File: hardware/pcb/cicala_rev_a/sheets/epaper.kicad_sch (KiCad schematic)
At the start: 23 parts, among them J2 FH12-24S-0.5SH, Q1 Si1308EDL, U6 TPS22917DBVR

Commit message: feat(hw): isolate the panel bus and ground the USB-C shell
The panel's logic pins could back-power an unpowered panel through its own
ESD diodes whenever firmware deasserted EPD_PWR_EN with an output still
driven. R27-R31 put 470 ohm in series with every MCU-driven panel line, which
caps the injected current at about 5.7 mA per pin against a 3.3 V output and
a diode drop. At 4 MHz into roughly 20 pF of connector and trace the added
rise time is about 21 ns, so the same parts double as the series-tuning
positions the review asked for; fit 0 ohm to remove them during bring-up.

R32 holds the panel in reset while EPD_3V3 is off and while the MCU pin is
high-impedance. 1 M draws 3.3 uA, and only when RESET is high, which happens
only with the panel already powered.

The nets either side of the resistors are named apart: EPD_* stays the GPIO
net that pin_contract.csv and the firmware refer to, PNL_* is the panel side.

The USB-C shell had a no-connect flag and no recorded rationale. The
enclosure is plastic and carries no chassis ground, so the shell's only
discharge path is to the board. R33 (0 ohm, fitted) makes that path direct;
C31 is the alternative for a DC-isolated shell.

Co-Authored-By: Claude Opus 5 <noreply@anthropic.com>
Claude-Session: https://claude.ai/code/session_01E5vy1HJsPztSk9nFw6j5Ko
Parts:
- added R32: 1M, Resistor_SMD:R_0603_1608Metric, symbol Device:R
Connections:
- net GND: now also R32.2
- net EPD_CLK renamed PNL_CLK
- net EPD_CS renamed PNL_CS
- net EPD_DC renamed PNL_DC
- net EPD_MOSI renamed PNL_MOSI
- net EPD_RESET renamed PNL_RESET
- net PNL_RESET: now also R32.1
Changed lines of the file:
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@@
 	(wire
 		(pts
-			(xy 30.48 149.86) (xy 33.02 149.86)
-		)
-		(stroke
-			(width 0)
-			(type default)
-		)
-	)
-	(wire
-		(pts
 			(xy 62.23 43.18) (xy 62.23 48.26)
 		)
@@
 		)
 	)
-	(global_label "EPD_MOSI"
+	(global_label "PNL_MOSI"
 		(shape passive)
 		(at 33.02 160.02 0)
@@
 		)
 	)
-	(global_label "EPD_CS"
+	(global_label "PNL_CS"
 		(shape passive)
 		(at 33.02 154.94 0)
@@
 		)
 	)
-	(global_label "EPD_CLK"
+	(global_label "PNL_CLK"
 		(shape passive)
 		(at 33.02 157.48 0)
@@
 		)
 	)
-	(global_label "EPD_DC"
+	(global_label "PNL_DC"
 		(shape passive)
 		(at 33.02 152.4 0)
@@
 		)
 	)
-	(global_label "EPD_RESET"
+	(global_label "PNL_RESET"
 		(shape passive)
-		(at 33.02 149.86 0)
+		(at 55.88 149.86 0)
 		(fields_autoplaced yes)
 		(effects
@@
 		)
 		(property "Intersheetrefs" "${INTERSHEET_REFS}"
-			(at 33.02 149.86 0)
+			(at 55.88 149.86 0)
 			(hide yes)
 			(show_name no)
@@
 				)
 			)
+		)
+	)
+	(wire
+		(pts
+			(xy 30.48 149.86) (xy 55.88 149.86)
+		)
+		(stroke
+			(width 0)
+			(type default)
+		)
+	)
+	(junction
+		(at 45.72 149.86)
+		(diameter 0)
+		(color 0 0 0 0)
+	)
+	(symbol
+		(lib_id "Device:R")
+		(at 45.72 153.67 0)
+		(unit 1)
+		(body_style 1)
+		(exclude_from_sim no)
+		(in_bom yes)
+		(on_board yes)
+		(in_pos_files yes)
+		(dnp no)
+		(property "Reference" "R32"
+			(at 41.91 151.892 0)
+			(show_name no)
+			(do_not_autoplace no)
+			(effects
+				(font
+					(size 1 1)
+				)
+			)
+		)
+		(property "Value" "1M"
+			(at 41.91 154.432 0)
+			(show_name no)
+			(do_not_autoplace no)
+			(effects
+				(font
+					(size 1 1)
+				)
+			)
+		)
+		(property "Footprint" "Resistor_SMD:R_0603_1608Metric"
+			(at 45.72 153.67 0)
+			(hide yes)
+			(show_name no)
+			(do_not_autoplace no)
+			(effects
+				(font
+					(size 1 1)
+				)
+			)
+		)
+		(property "Datasheet" "~"
+			(at 45.72 153.67 0)
+			(hide yes)
+			(show_name no)
+			(do_not_autoplace no)
+			(effects
+				(font
+					(size 1 1)
+				)
+			)
+		)
+		(property "Description" "Resistor"
+			(at 45.72 153.67 0)
+			(hide yes)
+			(show_name no)
+			(do_not_autoplace no)
+			(effects
+				(font
+					(size 1 1)
+				)
+			)
+		)
+		(pin "1"
+		)
+		(pin "2"
+		)
+		(instances
+			(project "cicala_rev_a"
+				(path "/9b5e4c31-c66f-4b64-9ff8-62a2c447d0bc/9467d62a-f8ed-46c9-a7cb-f7af887ddb15"
+					(reference "R32")
+					(unit 1)
+				)
+			)
+		)
+	)
+	(wire
+		(pts
+			(xy 45.72 157.48) (xy 45.72 160.02)
+		)
+		(stroke
+			(width 0)
+			(type default)
+		)
+	)
+	(symbol
+		(lib_id "power:GND")
+		(at 45.72 160.02 0)
+		(unit 1)
+		(body_style 1)
+		(exclude_from_sim no)
+		(in_bom yes)
+		(on_board yes)
+		(in_pos_files yes)
+		(dnp no)
+		(property "Reference" "#PWR0156"
+			(at 45.72 166.37 0)
+			(hide yes)
+			(show_name no)
+			(do_not_autoplace no)
+			(effects
+				(font
+					(size 1.27 1.27)
+				)
+			)
+		)
+		(property "Value" "GND"
+			(at 45.72 163.83 0)
+			(hide yes)
+			(show_name no)
+			(do_not_autoplace no)
+			(effects
+				(font
+					(size 1.27 1.27)
+				)
+			)
+		)
+		(property "Footprint" ""
+			(at 45.72 160.02 0)
+			(hide yes)
+			(show_name no)
+			(do_not_autoplace no)
+			(effects
+				(font
+					(size 1.27 1.27)
+				)
+			)
+		)
+		(property "Datasheet" ""
+			(at 45.72 160.02 0)
+			(hide yes)
+			(show_name no)
+			(do_not_autoplace no)
+			(effects
+				(font
+					(size 1.27 1.27)
+				)
+			)
+		)
+		(property "Description" "Power symbol creates a global label with name GND, ground"
+			(at 45.72 160.02 0)
+			(hide yes)
+			(show_name no)
+			(do_not_autoplace no)
+			(effects
+				(font
+					(size 1.27 1.27)
+				)
+			)
+		)
+		(pin "1"
+		)
+		(instances
+			(project "cicala_rev_a"
+				(path "/9b5e4c31-c66f-4b64-9ff8-62a2c447d0bc/9467d62a-f8ed-46c9-a7cb-f7af887ddb15"
+					(reference "#PWR0156")
+					(unit 1)
+				)
+			)

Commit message: feat(hw): give the panel a real symbol and name its pump rails
J2 was a generic Conn_01x24, so every panel signal was Pin_n and ERC could
not see an interface error. It is now a project GDEY0213B74 symbol carrying
the vendor pin names and electrical types: the four MCU-driven lines are
inputs, BUSY and GDR are outputs, VDDIO/VCI/VSS are power inputs. Pin
geometry is deliberately identical to Conn_01x24, so the sheet's wiring is
unchanged and the FH12-24S-0.5SH land still applies.

The pinout the sheet already had matches the vendor assignment on all 24
pins, including BS1 tied low for 4-wire SPI and VPP and the temperature-sensor
pair left open.

EPD_PREVGH and EPD_PREVGL are renamed EPD_VGH and EPD_VGL. They are not
pre-pump nodes: D3 rectifies the boost switch node into panel pin 21, and D1
with the C16 flying capacitor pumps panel pin 23 negative. The old names
describe the wrong side of the circuit, and one earlier wiring error on this
exact node was made easier by them.

Co-Authored-By: Claude Opus 5 <noreply@anthropic.com>
Claude-Session: https://claude.ai/code/session_01E5vy1HJsPztSk9nFw6j5Ko
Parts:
- J2: value FH12-24S-0.5SH -> GDEY0213B74; symbol Connector_Generic:Conn_01x24 -> Cicala:GDEY0213B74
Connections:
- net EPD_PREVGH renamed EPD_VGH
- net EPD_PREVGL renamed EPD_VGL
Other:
- moved on the sheet: J2
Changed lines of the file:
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@@
 		)
 	)
-	(global_label "EPD_PREVGL"
+	(global_label "EPD_VGL"
 		(shape passive)
 		(at 237.49 142.24 90)
@@
 		)
 	)
-	(global_label "EPD_PREVGH"
+	(global_label "EPD_VGH"
 		(shape passive)
 		(at 139.7 57.15 180)
@@
 		)
 	)
-	(global_label "EPD_PREVGH"
+	(global_label "EPD_VGH"
 		(shape passive)
 		(at 33.02 177.8 0)
@@
 		)
 	)
-	(global_label "EPD_PREVGL"
+	(global_label "EPD_VGL"
 		(shape passive)
 		(at 153.67 91.44 0)
@@
 		)
 	)
-	(global_label "EPD_PREVGH"
+	(global_label "EPD_VGH"
 		(shape passive)
 		(at 267.97 113.03 90)
@@
 		)
 	)
-	(global_label "EPD_PREVGL"
+	(global_label "EPD_VGL"
 		(shape passive)
 		(at 33.02 182.88 0)
@@
 	)
 	(symbol
-		(lib_id "Connector_Generic:Conn_01x24")
+		(lib_id "Cicala:GDEY0213B74")
 		(at 25.4 154.94 0)
 		(mirror y)
@@
 			)
 		)
-		(property "Value" "FH12-24S-0.5SH"
+		(property "Value" "GDEY0213B74"
 			(at 25.146 189.23 0)
 			(show_name no)
@@
 			)
 		)
-		(property "Description" "Generic connector, single row, 01x24, script generated (kicad-library-utils/schlib/autogen/connector/)"
+		(property "Description" "Panel and its FH12-24S-0.5SH board connector"
 			(at 25.4 154.94 0)
 			(hide yes)

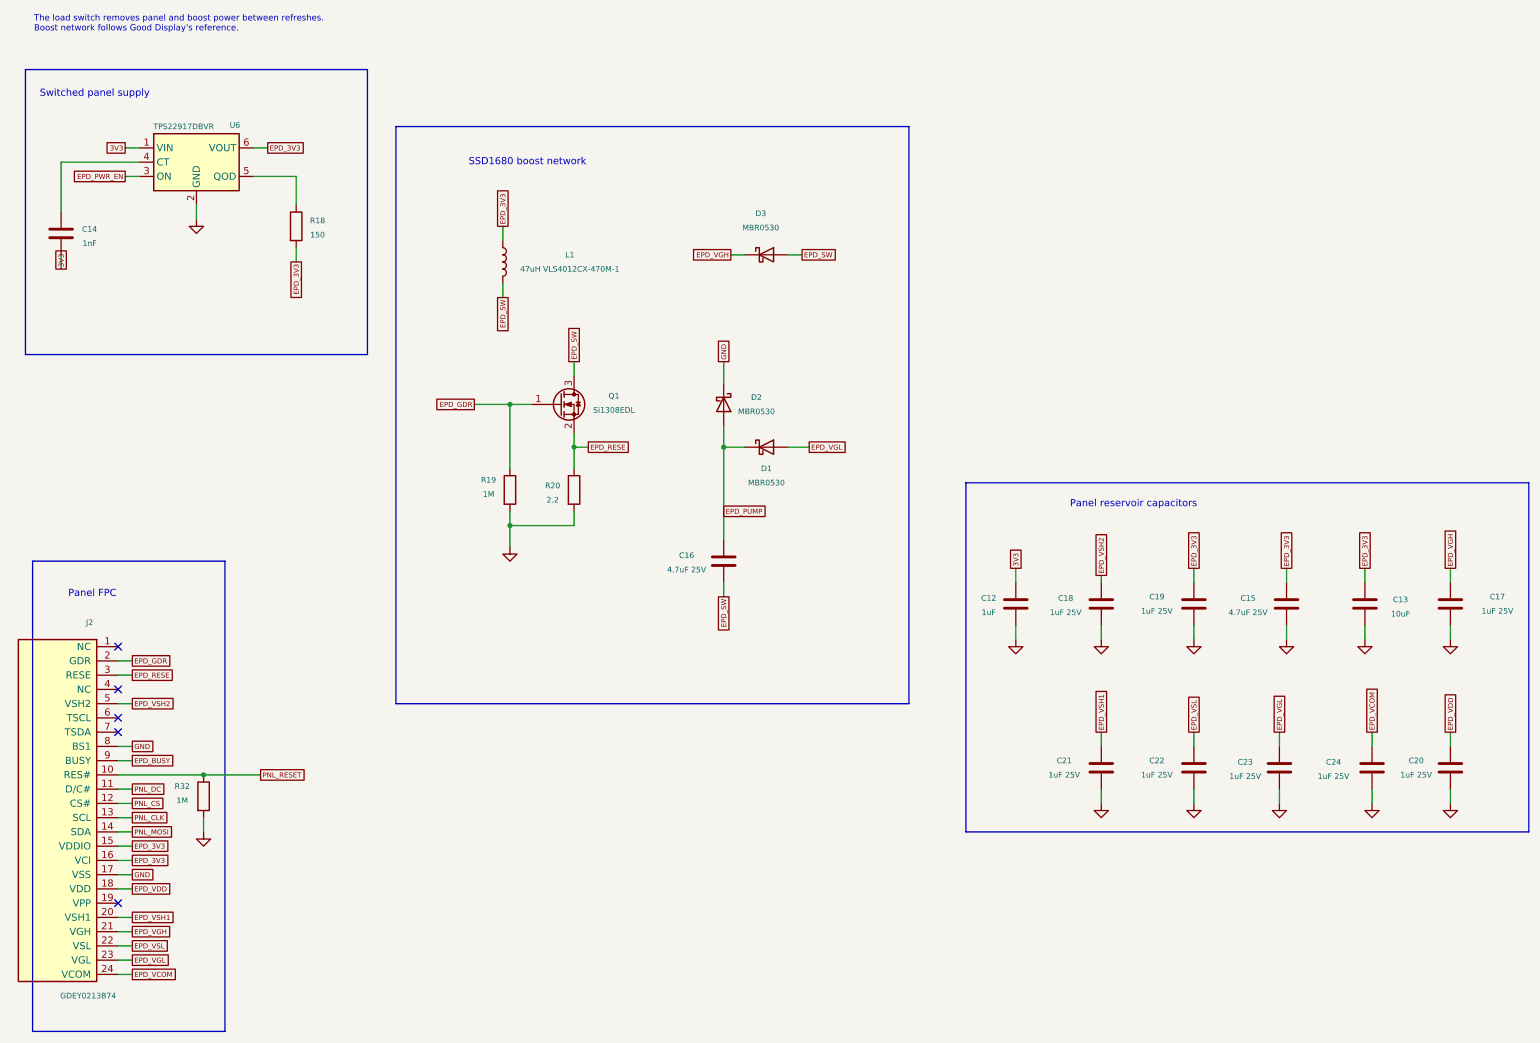
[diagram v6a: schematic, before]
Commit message: feat(hw): add the production test contract and a cell-current link
TP12-TP15 expose the USB pair and both charger status lines. TP16-TP21 expose
the panel side of the display bus, next to the isolation resistors that now
live on the panel sheet where the interface they protect is drawn.

R34 is a removable 0 ohm link in the cell lead, with TP22 on the pack side.
Lifting it puts a meter between the pack and everything else, which is the
only way to measure whole-device sleep current against the 30 uA target
without cutting a trace. No link is placed in a switching loop: VSYS and 3V3
stay unbroken and are probed at TP7 and TP9.

Co-Authored-By: Claude Opus 5 <noreply@anthropic.com>
Claude-Session: https://claude.ai/code/session_01E5vy1HJsPztSk9nFw6j5Ko
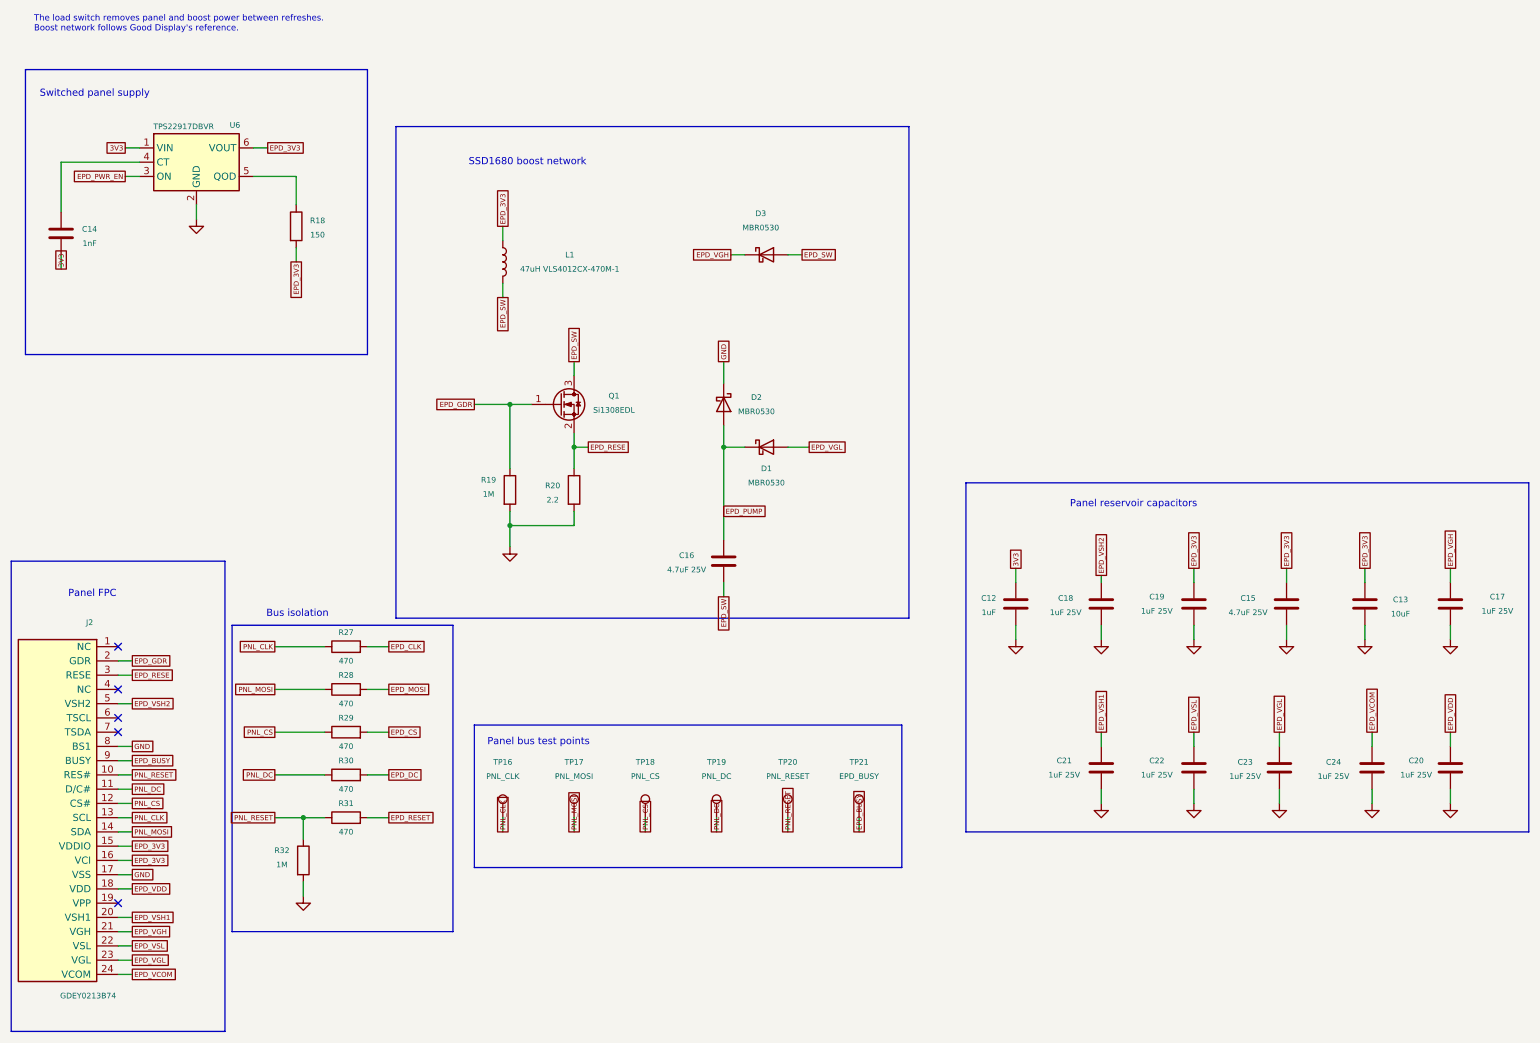
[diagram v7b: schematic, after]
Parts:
- added R27, R28, R29, R30, R31: 470, Resistor_SMD:R_0603_1608Metric, symbol Device:R
- added TP16: PNL_CLK, TestPoint:TestPoint_Pad_D1.0mm, symbol Connector:TestPoint
- added TP17: PNL_MOSI, TestPoint:TestPoint_Pad_D1.0mm, symbol Connector:TestPoint
- added TP18: PNL_CS, TestPoint:TestPoint_Pad_D1.0mm, symbol Connector:TestPoint
- added TP19: PNL_DC, TestPoint:TestPoint_Pad_D1.0mm, symbol Connector:TestPoint
- added TP20: PNL_RESET, TestPoint:TestPoint_Pad_D1.0mm, symbol Connector:TestPoint
- added TP21: EPD_BUSY, TestPoint:TestPoint_Pad_D1.0mm, symbol Connector:TestPoint
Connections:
- net EPD_BUSY: now also TP21.1
- net PNL_CLK: now also R27.1, TP16.1
- net PNL_CS: now also R29.1, TP18.1
- net PNL_DC: now also R30.1, TP19.1
- net PNL_MOSI: now also R28.1, TP17.1
- net PNL_RESET: now also R31.1, TP20.1
- new net EPD_CLK: R27.2
- new net EPD_CS: R29.2
- new net EPD_DC: R30.2
- new net EPD_MOSI: R28.2
- new net EPD_RESET: R31.2
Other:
- note added: "Bus isolation"
- note added: "Panel bus test points"
